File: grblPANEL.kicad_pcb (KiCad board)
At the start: 4 copper layers, 84 x 55 mm, 152 parts, among them J101 Conn_01x02, J201 2x5x1.27mm, J202 USB_C_Receptacle_USB2.0, J301 Conn_01x02, J401 Conn_01x02, J501 ILI9488, J601 Conn_02x10_Odd_Even, J701 Conn_01x04, J702 Conn_01x04, J703 Conn_01x04, J704 Conn_01x04, Q501 Q_NPN_BEC - S8050, SW201 SW_Push, SW202 SW_Push, U101 MAX17612A, U102 AZ1117-3.3, U201 STM32G0B1CxTxN, U202 USBLC6-2SC6, U301 SN65HVD230, U401 THVD1406, U601 ADP5589, Y201 8MHz

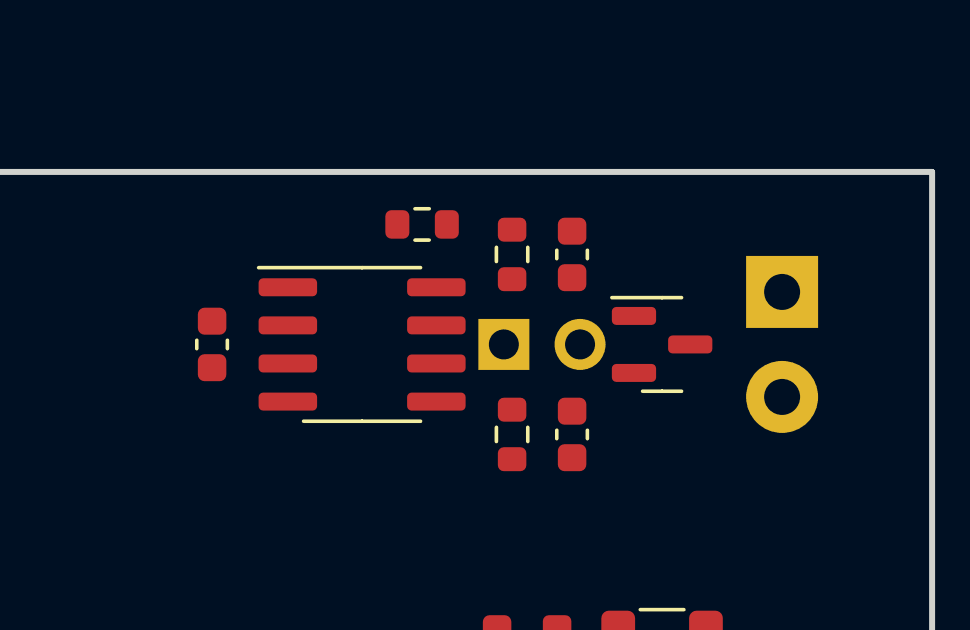
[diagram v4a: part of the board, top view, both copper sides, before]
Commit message: 1st stab at routing can interface
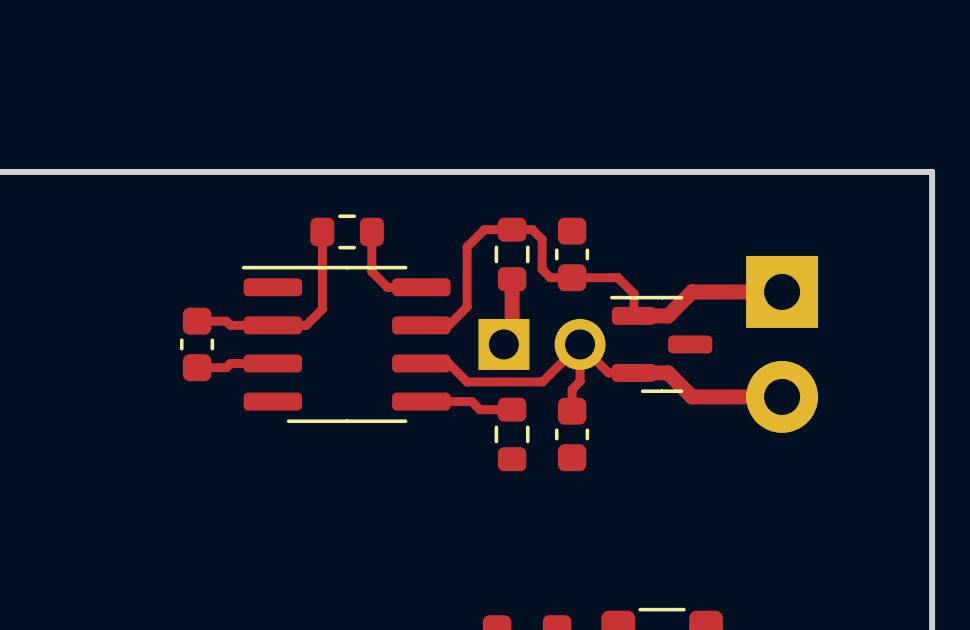
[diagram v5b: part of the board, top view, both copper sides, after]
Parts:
- moved R302 2.51 mm to (85.5, 131.0)
- moved C301 0.50 mm to (80.5, 134.8)
- moved U301 0.50 mm to (85.5, 134.8)
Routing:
- net /CAN bus/CONN_CANH: track 0.00 -> 17.3 mm
- net /CAN bus/CONN_CANL: track 0.00 -> 15.9 mm
- net GND: track 21.9 -> 28.9 mm
- net /CAN bus/CAN_RS: track 0.00 -> 3.19 mm
- net /CAN bus/CAN_VREF: track 0.00 -> 3.14 mm
- net +3V3: track 19.3 -> 21.9 mm
- net Net-(JP301-Pad1): track 0.00 -> 2.29 mm
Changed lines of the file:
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@@
   )
   (footprint "Capacitor_SMD:C_0603_1608Metric" (layer "F.Cu")
-    (at 81 134.75 90)
+    (at 80.5 134.75 90)
     (descr "Capacitor SMD 0603 (1608 Metric), square (rectangular) end terminal, IPC_7351 nominal, (Body size source: IPC-SM-782 page 76, https://www.pcb-3d.com/wordpress/wp-content/uploads/ipc-sm-782a_amendment_1_and_2.pdf), generated with kicad-footprint-generator")
     (tags "capacitor")
@@
   )
   (footprint "Resistor_SMD:R_0603_1608Metric" (layer "F.Cu")
-    (at 88 130.75 180)
+    (at 85.5 131 180)
     (descr "Resistor SMD 0603 (1608 Metric), square (rectangular) end terminal, IPC_7351 nominal, (Body size source: IPC-SM-782 page 72, https://www.pcb-3d.com/wordpress/wp-content/uploads/ipc-sm-782a_amendment_1_and_2.pdf), generated with kicad-footprint-generator")
     (tags "resistor")
@@
   )
   (footprint "Package_SO:SOIC-8_3.9x4.9mm_P1.27mm" (layer "F.Cu")
-    (at 86 134.75)
+    (at 85.5 134.75)
     (descr "SOIC, 8 Pin (JEDEC MS-012AA, https://www.analog.com/media/en/package-pcb-resources/package/pkg_pdf/soic_narrow-r/r_8.pdf), generated with kicad-footprint-generator ipc_gullwing_generator.py")
     (tags "SOIC SO")
@@
     (effects (font (size 1.5 1.3) (thickness 0.2)) (justify mirror))
   )
-  (gr_text "CAN\nTERM" (at 86.5 135) (layer "B.SilkS")
+  (gr_text "CAN\nTERM" (at 86 135) (layer "B.SilkS")
     (effects (font (size 1.5 1.3) (thickness 0.2)) (justify mirror))
   )
@@
   (segment (start 85.975 181.475) (end 86 181.5) (width 0.5) (layer "F.Cu") (net 2))
   (segment (start 86.15 171.8) (end 88.175 171.8) (width 0.5) (layer "F.Cu") (net 2))
+  (segment (start 81.475 133.975) (end 80.5 133.975) (width 0.3) (layer "F.Cu") (net 2))
+  (segment (start 81.615 134.115) (end 81.475 133.975) (width 0.3) (layer "F.Cu") (net 2))
   (segment (start 88.5 180.2) (end 88.5 181.5) (width 0.5) (layer "F.Cu") (net 2))
   (segment (start 89.475 170.975) (end 90 171.5) (width 0.5) (layer "F.Cu") (net 2))
+  (segment (start 84.135 134.115) (end 84.675 133.575) (width 0.3) (layer "F.Cu") (net 2))
   (segment (start 83.0038 175.999999) (end 82.250001 175.999999) (width 0.15) (layer "F.Cu") (net 2))
   (segment (start 95.5 175.25) (end 95.5 173) (width 0.5) (layer "F.Cu") (net 2))
+  (segment (start 83.025 134.115) (end 81.615 134.115) (width 0.3) (layer "F.Cu") (net 2))
   (segment (start 92.225 168.5) (end 91.201376 168.5) (width 0.5) (layer "F.Cu") (net 2))
   (segment (start 90.5 172) (end 91 172) (width 0.5) (layer "F.Cu") (net 2))
   (segment (start 88.5 174.425) (end 88.5 173) (width 0.5) (layer "F.Cu") (net 2))
+  (segment (start 84.675 133.575) (end 84.675 131) (width 0.3) (layer "F.Cu") (net 2))
   (segment (start 81 176.325) (end 81 177.5) (width 0.15) (layer "F.Cu") (net 2))
+  (segment (start 83.025 134.115) (end 84.135 134.115) (width 0.3) (layer "F.Cu") (net 2))
   (segment (start 90 171.5) (end 90.5 172) (width 0.5) (layer "F.Cu") (net 2))
   (segment (start 91.201376 168.5) (end 91.100688 168.600688) (width 0.5) (layer "F.Cu") (net 2))
@@
   (segment (start 86.15 167.2) (end 88.175 167.2) (width 0.5) (layer "F.Cu") (net 5))
   (segment (start 94.5 167) (end 91.5 167) (width 0.5) (layer "F.Cu") (net 5))
+  (segment (start 83.025 135.385) (end 81.615 135.385) (width 0.3) (layer "F.Cu") (net 6))
+  (segment (start 81.615 135.385) (end 81.475 135.525) (width 0.3) (layer "F.Cu") (net 6))
   (segment (start 86.15 169.5) (end 79.85 169.5) (width 0.5) (layer "F.Cu") (net 6))
   (segment (start 78.5 169.5) (end 79.85 169.5) (width 0.5) (layer "F.Cu") (net 6))
   (segment (start 79 178.7125) (end 79 174.5) (width 0.3) (layer "F.Cu") (net 6))
+  (segment (start 81.475 135.525) (end 80.5 135.525) (width 0.3) (layer "F.Cu") (net 6))
   (segment (start 77.025 168.025) (end 78.5 169.5) (width 0.5) (layer "F.Cu") (net 6))
   (segment (start 79.85 173.65) (end 79.85 169.5) (width 0.3) (layer "F.Cu") (net 6))
@@
   (segment (start 80.9625 180.2875) (end 81 180.325) (width 0.5) (layer "F.Cu") (net 12))
   (segment (start 79 180.2875) (end 80.9625 180.2875) (width 0.5) (layer "F.Cu") (net 12))
+  (segment (start 91 132.575) (end 91 134.475) (width 0.5) (layer "F.Cu") (net 64))
+  (segment (start 91 134.475) (end 90.725 134.75) (width 0.5) (layer "F.Cu") (net 64))
   (segment (start 85.9962 175.999999) (end 86.499999 175.999999) (width 0.15) (layer "F.Cu") (net 68))
   (segment (start 86.85 176.35) (end 86.85 176.665686) (width 0.15) (layer "F.Cu") (net 68))
@@
   (segment (start 83.0038 175.5) (end 81.25 175.5) (width 0.15) (layer "F.Cu") (net 71))
   (segment (start 81 175.25) (end 81 174.675) (width 0.15) (layer "F.Cu") (net 71))
+  (segment (start 96.2 133.8) (end 95.0625 133.8) (width 0.5) (layer "F.Cu") (net 119))
+  (segment (start 88.885 134.115) (end 89.5 133.5) (width 0.3) (layer "F.Cu") (net 119))
+  (segment (start 100 133) (end 97 133) (width 0.5) (layer "F.Cu") (net 119))
+  (segment (start 89.5 133.5) (end 89.5 131.5) (width 0.3) (layer "F.Cu") (net 119))
+  (segment (start 97 133) (end 96.2 133.8) (width 0.5) (layer "F.Cu") (net 119))
+  (segment (start 90.075 130.925) (end 91 130.925) (width 0.3) (layer "F.Cu") (net 119))
+  (segment (start 87.975 134.115) (end 88.885 134.115) (width 0.3) (layer "F.Cu") (net 119))
+  (segment (start 92.275 132.525) (end 93 132.525) (width 0.3) (layer "F.Cu") (net 119))
+  (segment (start 94.525 132.525) (end 95.0625 133.0625) (width 0.3) (layer "F.Cu") (net 119))
+  (segment (start 92 131.25) (end 92 132.25) (width 0.3) (layer "F.Cu") (net 119))
+  (segment (start 91 130.925) (end 91.675 130.925) (width 0.3) (layer "F.Cu") (net 119))
+  (segment (start 92 132.25) (end 92.275 132.525) (width 0.3) (layer "F.Cu") (net 119))
+  (segment (start 95.0625 133.8) (end 94.8 133.8) (width 0.5) (layer "F.Cu") (net 119))
+  (segment (start 91.675 130.925) (end 92 131.25) (width 0.3) (layer "F.Cu") (net 119))
+  (segment (start 93 132.525) (end 94.525 132.525) (width 0.3) (layer "F.Cu") (net 119))
+  (segment (start 89.5 131.5) (end 90.075 130.925) (width 0.3) (layer "F.Cu") (net 119))
+  (segment (start 95.0625 133.0625) (end 95.0625 133.8) (width 0.3) (layer "F.Cu") (net 119))
+  (segment (start 92.015 136) (end 93.265 134.75) (width 0.3) (layer "F.Cu") (net 120))
+  (segment (start 96.2 135.7) (end 95.0625 135.7) (width 0.5) (layer "F.Cu") (net 120))
+  (segment (start 100 136.5) (end 97 136.5) (width 0.5) (layer "F.Cu") (net 120))
+  (segment (start 97 136.5) (end 96.2 135.7) (width 0.5) (layer "F.Cu") (net 120))
+  (segment (start 93.265 134.75) (end 93.265 135.985) (width 0.3) (layer "F.Cu") (net 120))
+  (segment (start 87.975 135.385) (end 88.885 135.385) (width 0.3) (layer "F.Cu") (net 120))
+  (segment (start 95.0125 135.75) (end 95.0625 135.7) (width 0.3) (layer "F.Cu") (net 120))
+  (segment (start 95.0625 135.7) (end 94.215 135.7) (width 0.3) (layer "F.Cu") (net 120))
+  (segment (start 88.885 135.385) (end 89.5 136) (width 0.3) (layer "F.Cu") (net 120))
+  (segment (start 93.265 135.985) (end 93 136.25) (width 0.3) (layer "F.Cu") (net 120))
+  (segment (start 93 136.25) (end 93 136.975) (width 0.3) (layer "F.Cu") (net 120))
+  (segment (start 89.5 136) (end 92.015 136) (width 0.3) (layer "F.Cu") (net 120))
+  (segment (start 94.215 135.7) (end 93.265 134.75) (width 0.3) (layer "F.Cu") (net 120))
+  (segment (start 91 136.925) (end 89.925 136.925) (width 0.3) (layer "F.Cu") (net 121))
+  (segment (start 89.925 136.925) (end 89.655 136.655) (width 0.3) (layer "F.Cu") (net 121))
+  (segment (start 87.975 136.655) (end 89.655 136.655) (width 0.3) (layer "F.Cu") (net 121))
+  (segment (start 86.325 132.325) (end 86.325 131) (width 0.3) (layer "F.Cu") (net 122))
+  (segment (start 86.845 132.845) (end 86.325 132.325) (width 0.3) (layer "F.Cu") (net 122))
+  (segment (start 87.975 132.845) (end 86.845 132.845) (width 0.3) (layer "F.Cu") (net 122))
   (zone (net 2) (net_name "GND") (layers "In1.Cu" "In2.Cu") (hatch edge 0.508)
     (connect_pads (clearance 0.508))

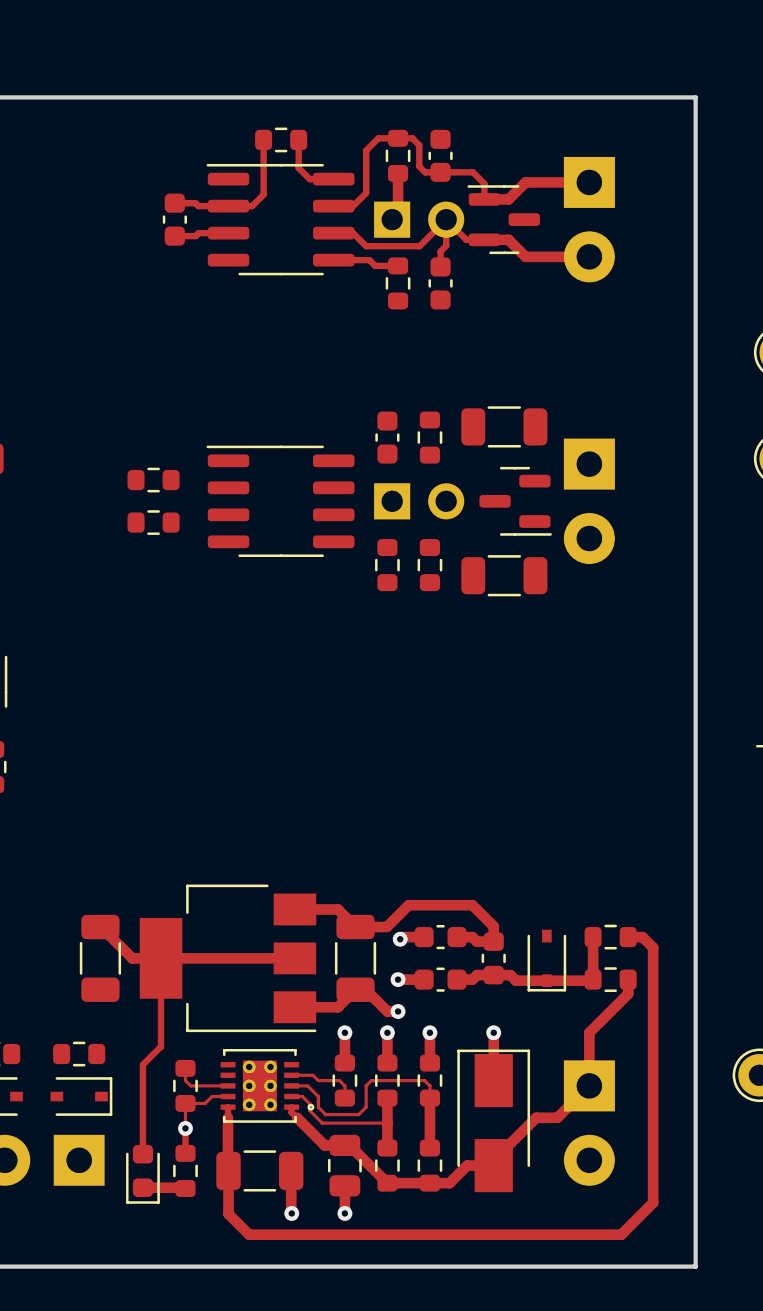
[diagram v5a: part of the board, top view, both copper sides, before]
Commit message: 1st stab at modbus interface routing
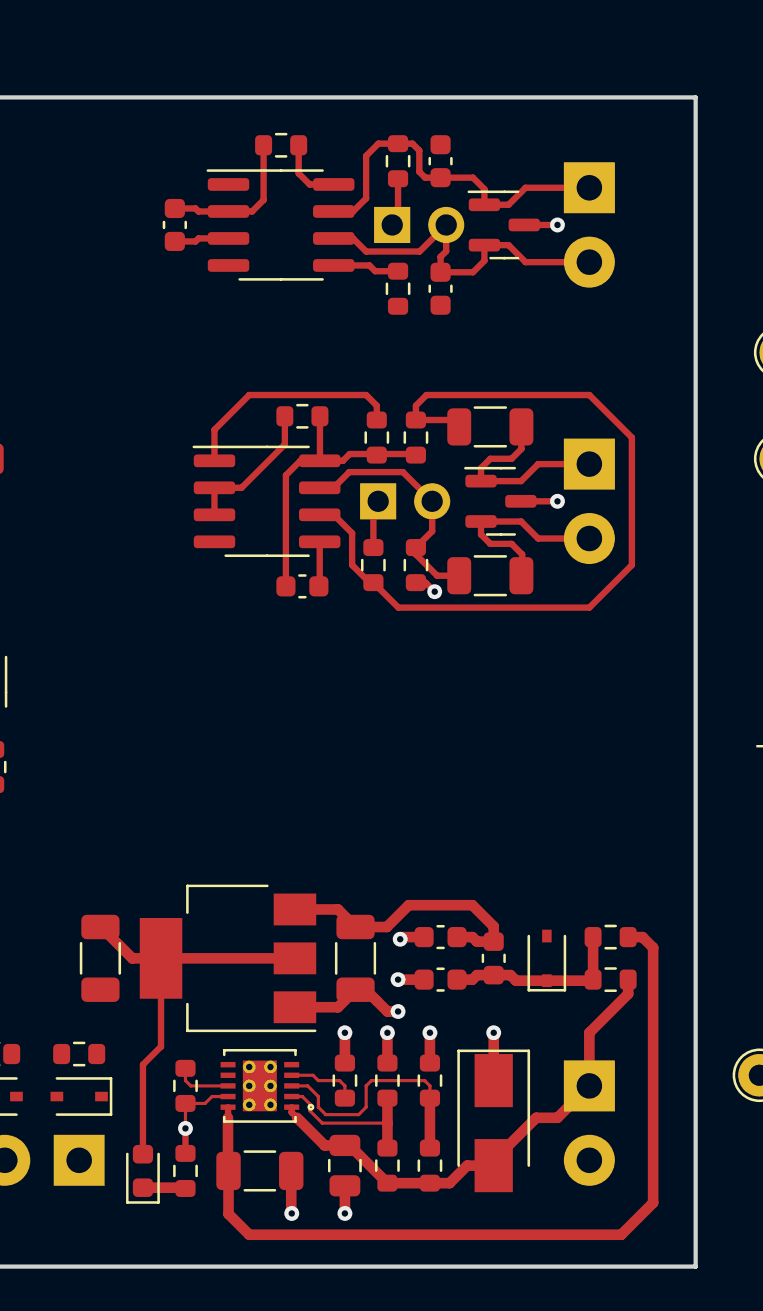
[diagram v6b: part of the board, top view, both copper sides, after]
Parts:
- moved R402 10.7 mm to (90.0, 145.0), turned to 90 degrees
- moved R401 8.60 mm to (86.5, 144.0), turned to 180 degrees
- moved C401 8.06 mm to (86.5, 152.0), turned to 0 degrees
- moved R406 7.03 mm to (95.3, 144.5)
- moved R407 7.03 mm to (95.3, 151.5)
- moved R404 6.04 mm to (91.8, 145.0)
- moved R405 6.04 mm to (91.8, 151.0), turned to -90 degrees
- moved D401 0.66 mm to (95.8, 148.0), turned to 0 degrees
- moved JP401 0.66 mm to (90.1, 148.0)
- moved R403 0.66 mm to (89.8, 151.0)
- moved U401 0.66 mm to (84.8, 148.0)
- moved C301 0.25 mm to (80.5, 135.0)
- moved C302 0.25 mm to (93.0, 132.0)
- moved C303 0.25 mm to (93.0, 138.0)
- moved D301 0.25 mm to (96.0, 135.0)
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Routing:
- net /Modbus/RS485_A: track 0.00 -> 36.9 mm
- net +3V3: track 21.9 -> 35.7 mm
- net /Modbus/RS485_B: track 0.00 -> 10.8 mm
- net MODBUS_RX: track 0.00 -> 10.7 mm
- net /Modbus/CONN_RS485_A: track 0.00 -> 9.35 mm
- net /Modbus/CONN_RS485_B: track 0.00 -> 9.33 mm
- net GND: track 28.9 -> 35.8 mm, vias 11 -> 14
- net /Modbus/RS485_MODE_SELECT: track 0.00 -> 6.75 mm
- net Net-(JP401-Pad1): track 0.00 -> 1.95 mm
- net /CAN bus/CONN_CANL: track 15.9 -> 16.7 mm

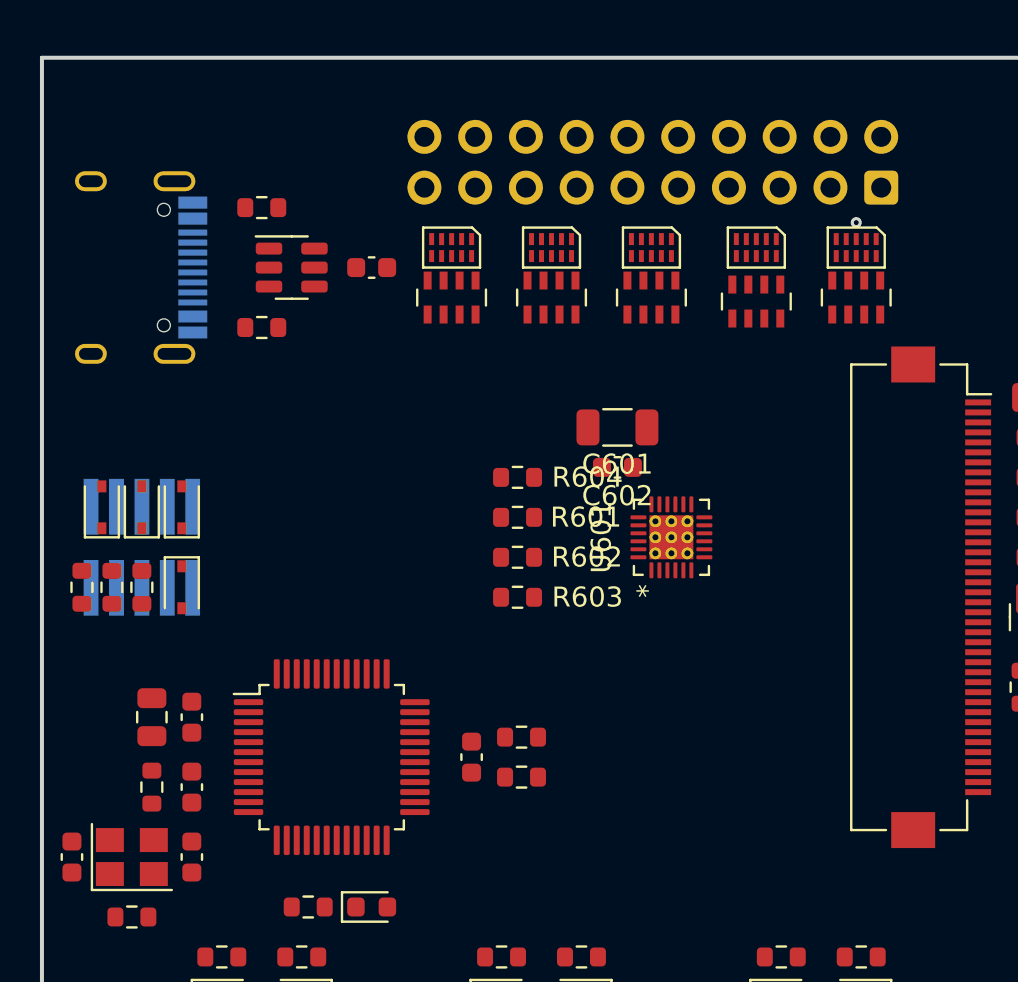
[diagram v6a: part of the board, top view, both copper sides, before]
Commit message: 1st stab at keypad + usb routing
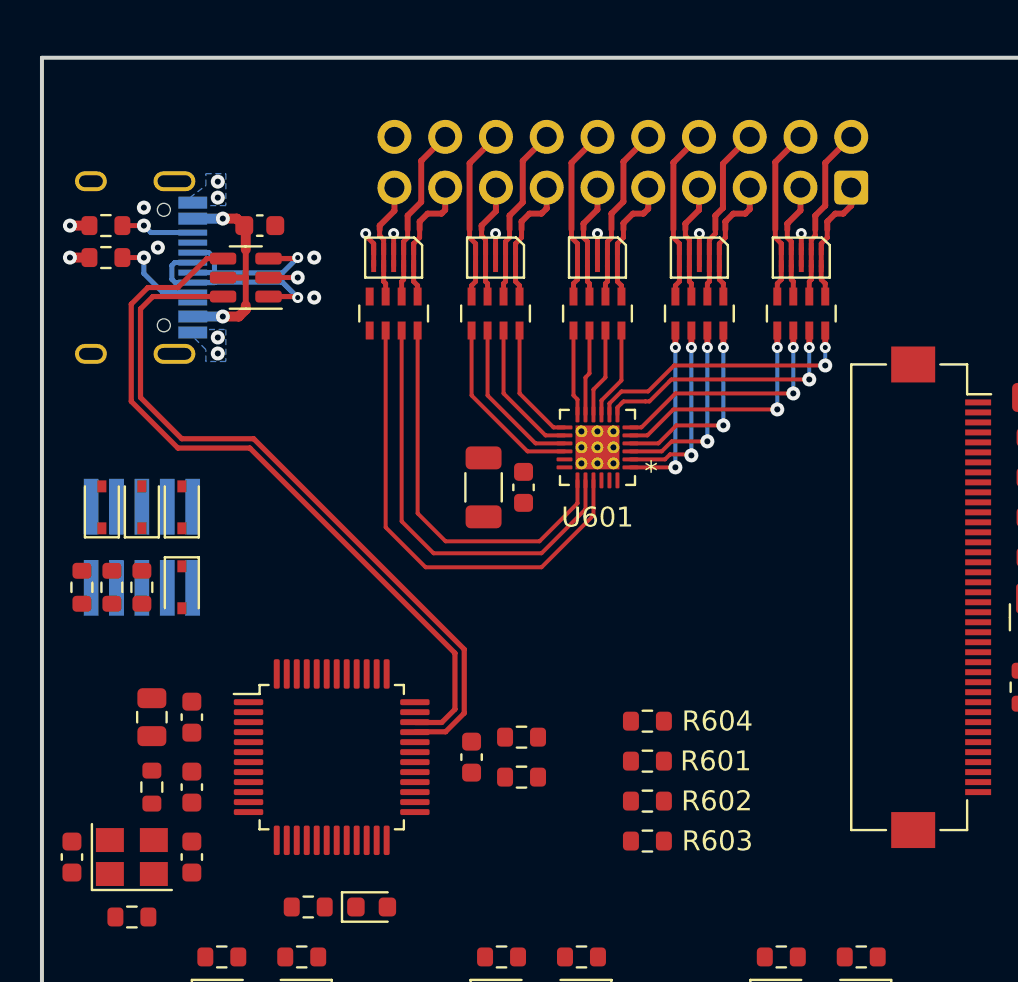
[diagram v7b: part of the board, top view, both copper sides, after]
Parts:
- moved R601 13.8 mm to (51.3, 164.2)
- moved R602 13.8 mm to (51.3, 166.2)
- moved R603 13.8 mm to (51.3, 168.2)
- moved R604 13.8 mm to (51.3, 162.2)
- moved R208 9.32 mm to (24.2, 137.4), turned to 180 degrees
- moved R207 8.19 mm to (24.2, 139.0)
- moved C601 7.34 mm to (43.1, 150.5), turned to -90 degrees
- moved C208 5.98 mm to (31.9, 137.4)
- moved U601 5.83 mm to (48.8, 148.5), turned to 180 degrees
- moved C602 4.81 mm to (45.1, 150.5), turned to -90 degrees
- moved RN605 3.01 mm to (38.6, 141.8)
- moved D605 2.94 mm to (38.6, 139.0)
- moved RN602 2.91 mm to (53.9, 141.8)
- moved RN604 2.91 mm to (43.7, 141.8)
- moved D602 2.89 mm to (53.9, 139.0)
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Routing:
- net /MCU/USB_D+: track 0.00 -> 36.9 mm
- net /MCU/USB_D-: track 0.00 -> 36.3 mm
- net /Keypad/C10: track 0.00 -> 23.9 mm
- net /Keypad/C9: track 0.00 -> 21.8 mm
- net /Keypad/C8: track 0.00 -> 19.7 mm
- net /Keypad/R0: track 0.00 -> 13.9 mm, vias 0 -> 2
- net GND: track 35.8 -> 49.0 mm, vias 14 -> 30
- net /Keypad/R1: track 0.00 -> 13.0 mm, vias 0 -> 2
- net /Keypad/R2: track 0.00 -> 12.0 mm, vias 0 -> 2
- net /Keypad/R3: track 0.00 -> 11.8 mm, vias 0 -> 2
- net VBUS: track 0.00 -> 10.9 mm, vias 0 -> 2
- net /MCU/USB_CONN_D-: track 0.00 -> 9.97 mm, vias 0 -> 1
- net /Keypad/R4: track 0.00 -> 9.77 mm, vias 0 -> 2
- net /Keypad/R5: track 0.00 -> 9.61 mm, vias 0 -> 2
- net /Keypad/R6: track 0.00 -> 9.42 mm, vias 0 -> 2
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- added copper zone on B.Cu, net GND

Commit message: bit more usb..
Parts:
- moved R207 7.77 mm to (28.6, 145.4), turned to 0 degrees
- moved R208 5.81 mm to (28.6, 133.6), turned to 0 degrees
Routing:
- net /MCU/USB_CONN_CC2: track 3.66 -> 7.57 mm
- net /MCU/USB_CONN_CC1: track 4.71 -> 8.07 mm
- net GND: vias 30 -> 28
